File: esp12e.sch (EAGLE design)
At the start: 32 parts, among them IC1 117\33

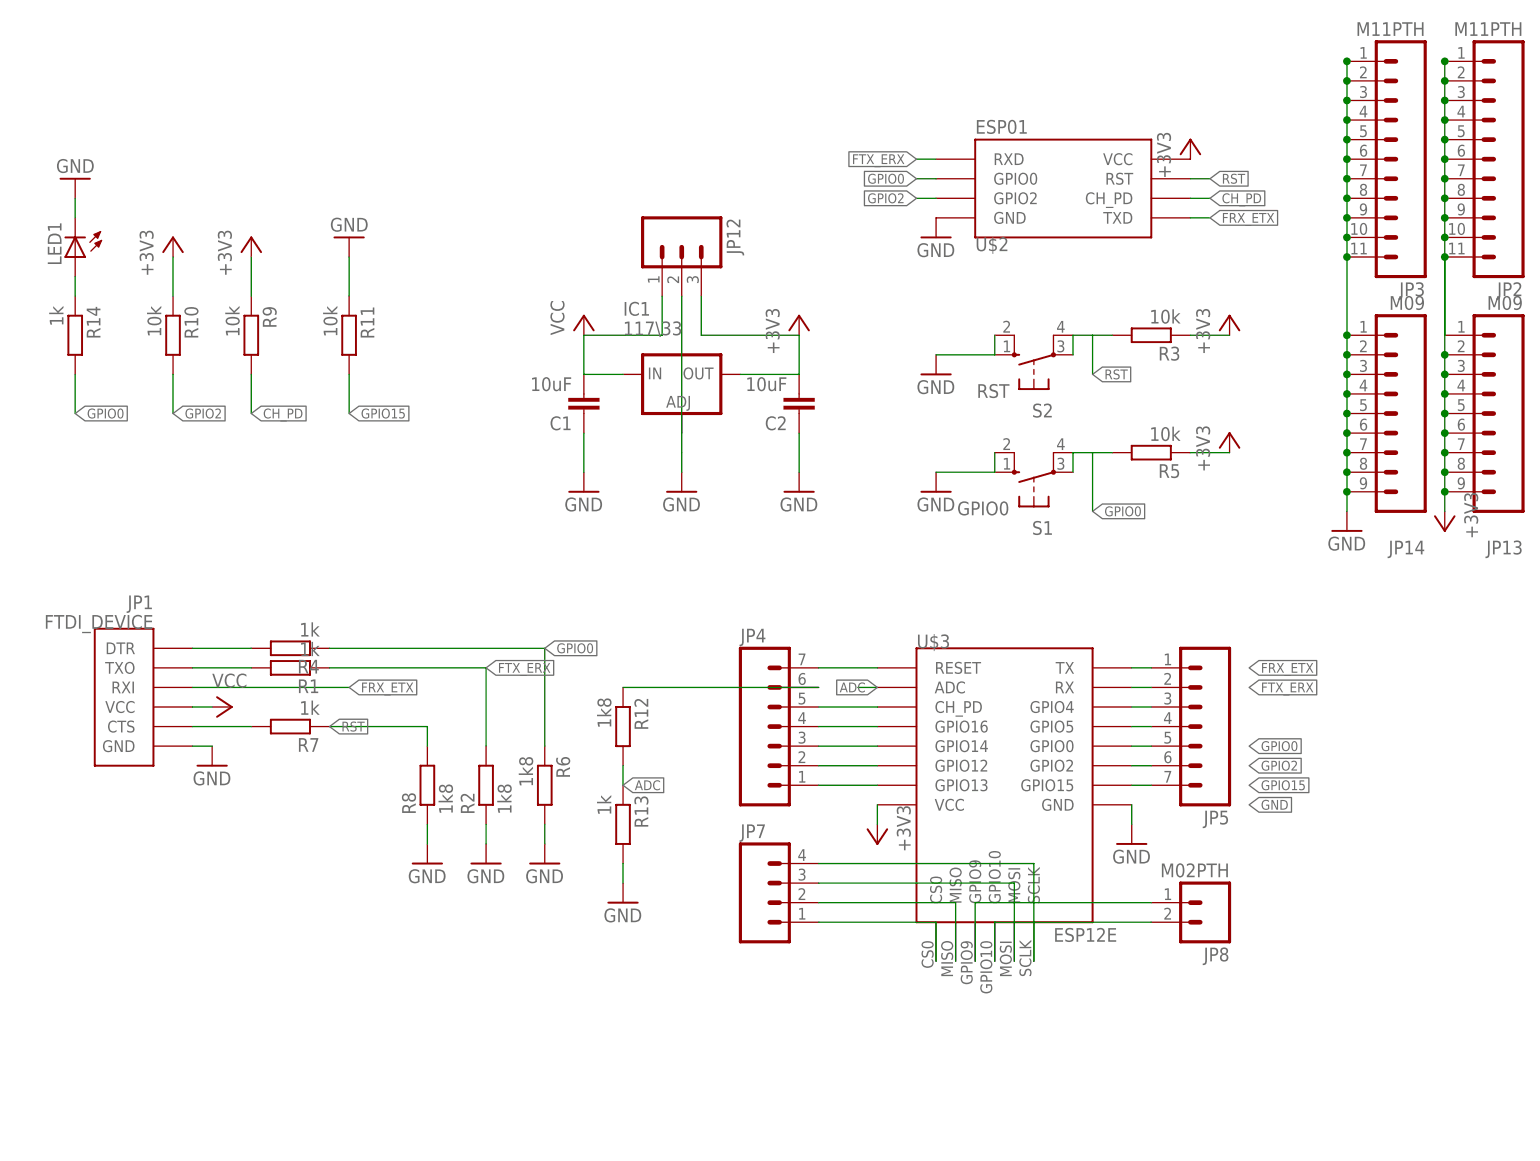
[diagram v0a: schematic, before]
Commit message: ISP AVR header - may be changed again
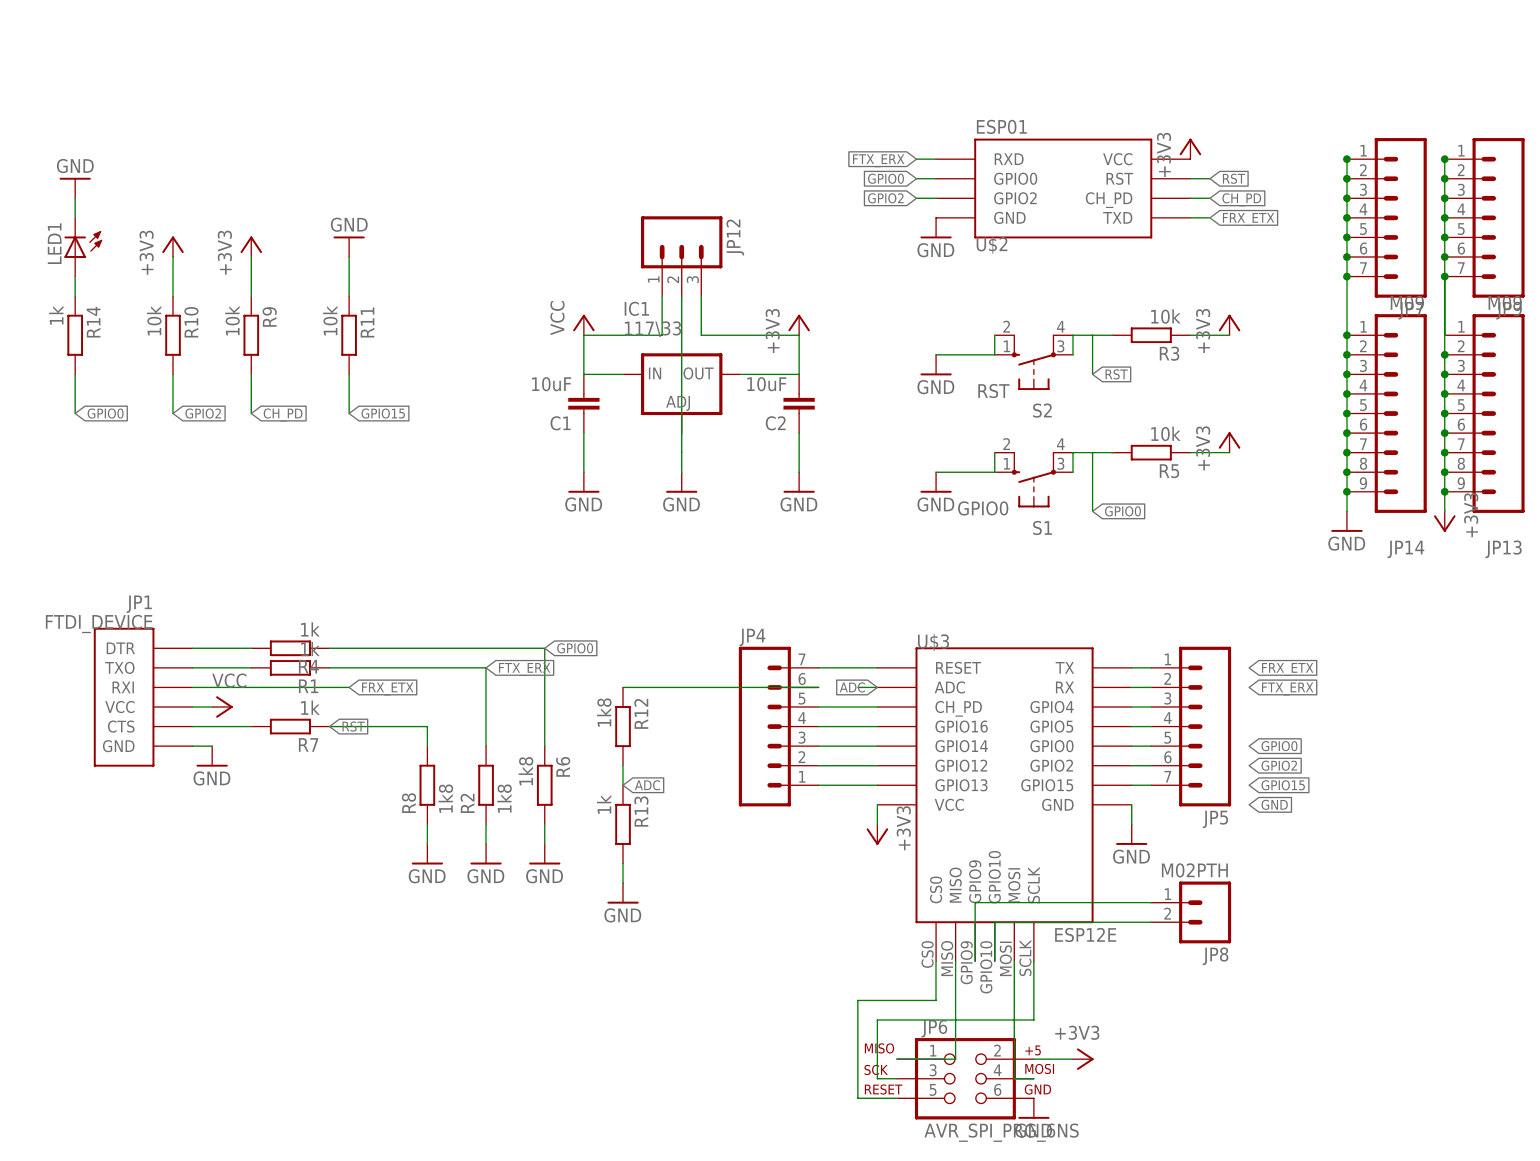
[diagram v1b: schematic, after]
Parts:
- removed JP2, JP3: M11PTH, SparkFun-Connectors:M11PTH
- added JP6: AVR_SPI_PRG_6NS, SparkFun-Connectors:AVR_SPI_PRG_6NS
- added JP9: (no value), SparkFun-Connectors:M07
- JP7: device SparkFun-Connectors:M041X04_NO_SILK -> SparkFun-Connectors:M07
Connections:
- net +3V3: now also JP6.2, JP9.1, JP9.2, JP9.3, JP9.4, JP9.5, JP9.6, JP9.7; no longer JP2.1, JP2.10, JP2.11, JP2.2, JP2.3, JP2.4, JP2.5, JP2.6, JP2.7, JP2.8, JP2.9
- net GND: now also JP6.6, JP7.1, JP7.2, JP7.3, JP7.4, JP7.5, JP7.6, JP7.7; no longer JP3.1, JP3.10, JP3.11, JP3.2, JP3.3, JP3.4, JP3.5, JP3.6, JP3.7, JP3.8, JP3.9
- net N$10: now also JP6.1, U$3.MISO; no longer JP7.1, U$3.CS0
- net N$11: now also JP6.4, U$3.MOSI; no longer JP7.2, U$3.MISO
- net N$12: now also JP6.3, U$3.SCLK; no longer JP7.3, U$3.MOSI
- net N$13: now also JP6.5, U$3.CS0; no longer JP7.4, U$3.SCLK

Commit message: hackaday swag
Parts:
- JP6: value AVR_SPI_PRG_6NS -> AVR_SPI
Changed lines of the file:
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@@
 <part name="JP13" library="SparkFun-Connectors" deviceset="M09" device=""/>
 <part name="JP14" library="SparkFun-Connectors" deviceset="M09" device=""/>
-<part name="JP6" library="SparkFun-Connectors" deviceset="AVR_SPI_PRG_6" device="NS"/>
+<part name="JP6" library="SparkFun-Connectors" deviceset="AVR_SPI_PRG_6" device="NS" value="AVR_SPI"/>
 <part name="JP7" library="SparkFun-Connectors" deviceset="M07" device=""/>
 <part name="JP9" library="SparkFun-Connectors" deviceset="M07" device=""/>

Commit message: 100nF because of regulator
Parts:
- C1: value 10uF -> 100nF
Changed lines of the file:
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@@
 <parts>
 <part name="IC1" library="v-reg" deviceset="LD117A?*" device="S" technology="33TR" value="117\33"/>
-<part name="C1" library="resistor" deviceset="C-EU" device="C1206" value="10uF"/>
+<part name="C1" library="resistor" deviceset="C-EU" device="C1206" value="100nF"/>
 <part name="C2" library="resistor" deviceset="C-EU" device="C1206" value="10uF"/>
 <part name="+3V1" library="supply1" deviceset="+3V3" device=""/>

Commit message: shield added
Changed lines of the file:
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@@
 <pinref part="U$3" gate="G$1" pin="CH_PD"/>
 <pinref part="JP4" gate="G$1" pin="5"/>
+<label x="40.64" y="43.18" size="1.27" layer="95" rot="R180" xref="yes"/>
 </segment>
 <segment>
